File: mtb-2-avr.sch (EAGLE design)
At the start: 1 part

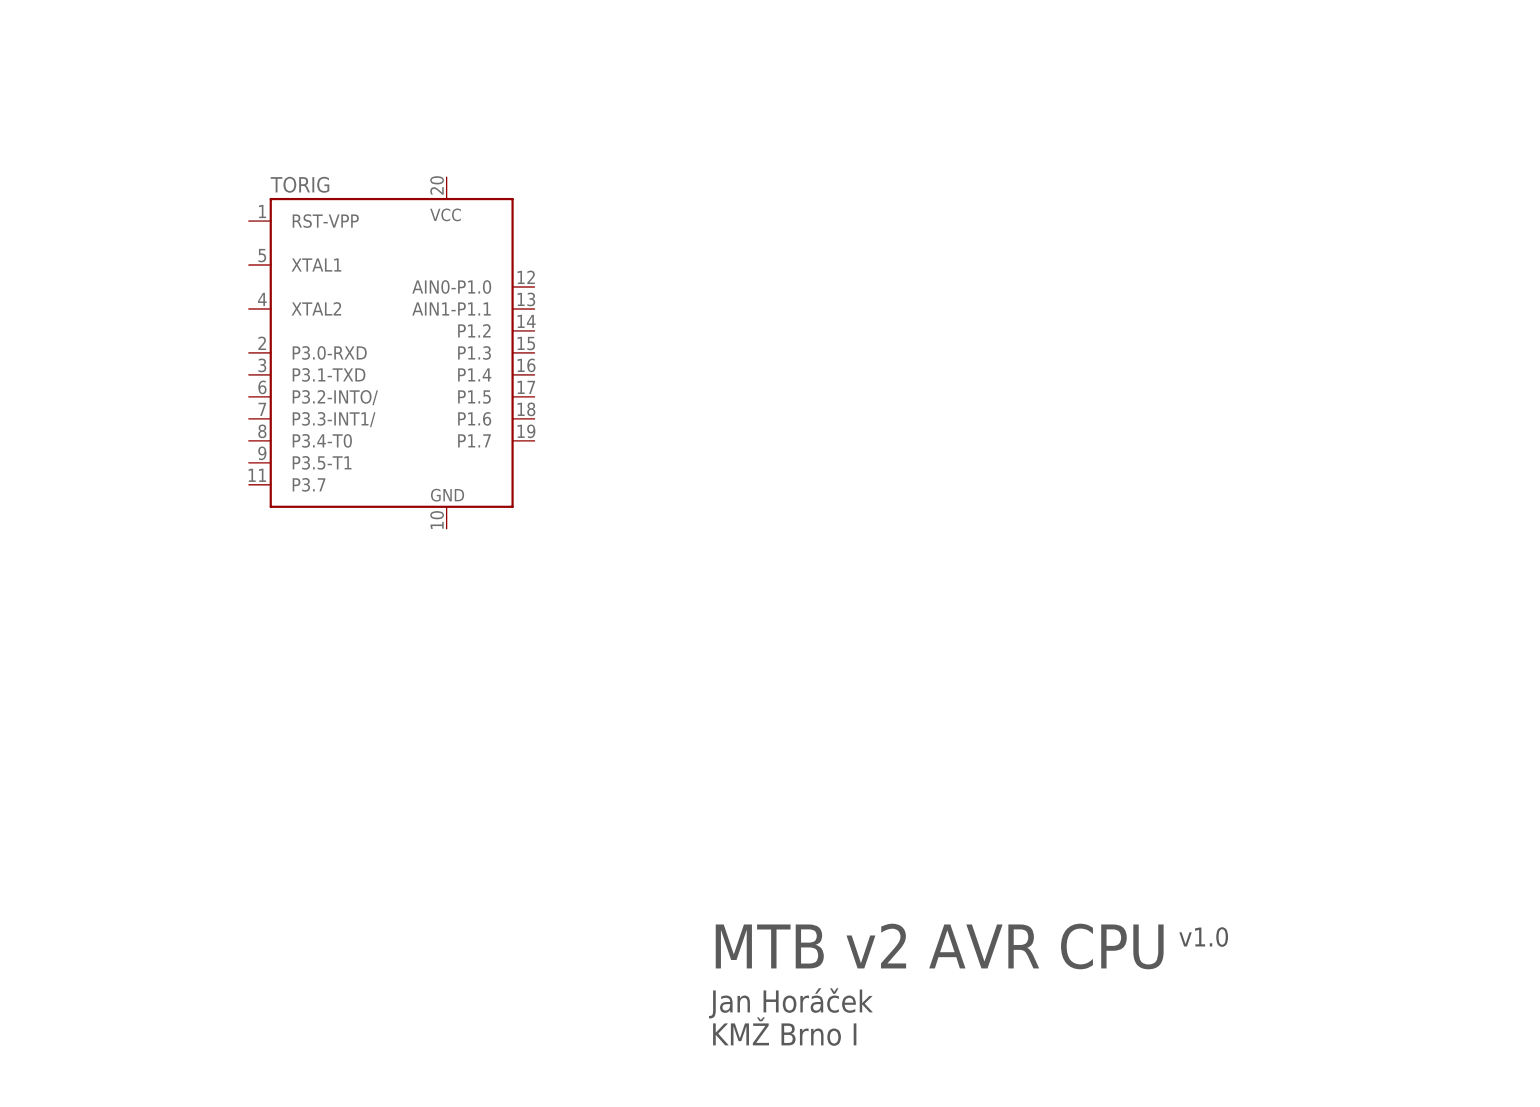
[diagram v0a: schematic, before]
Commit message: Add wires to schematics, create pcb template.
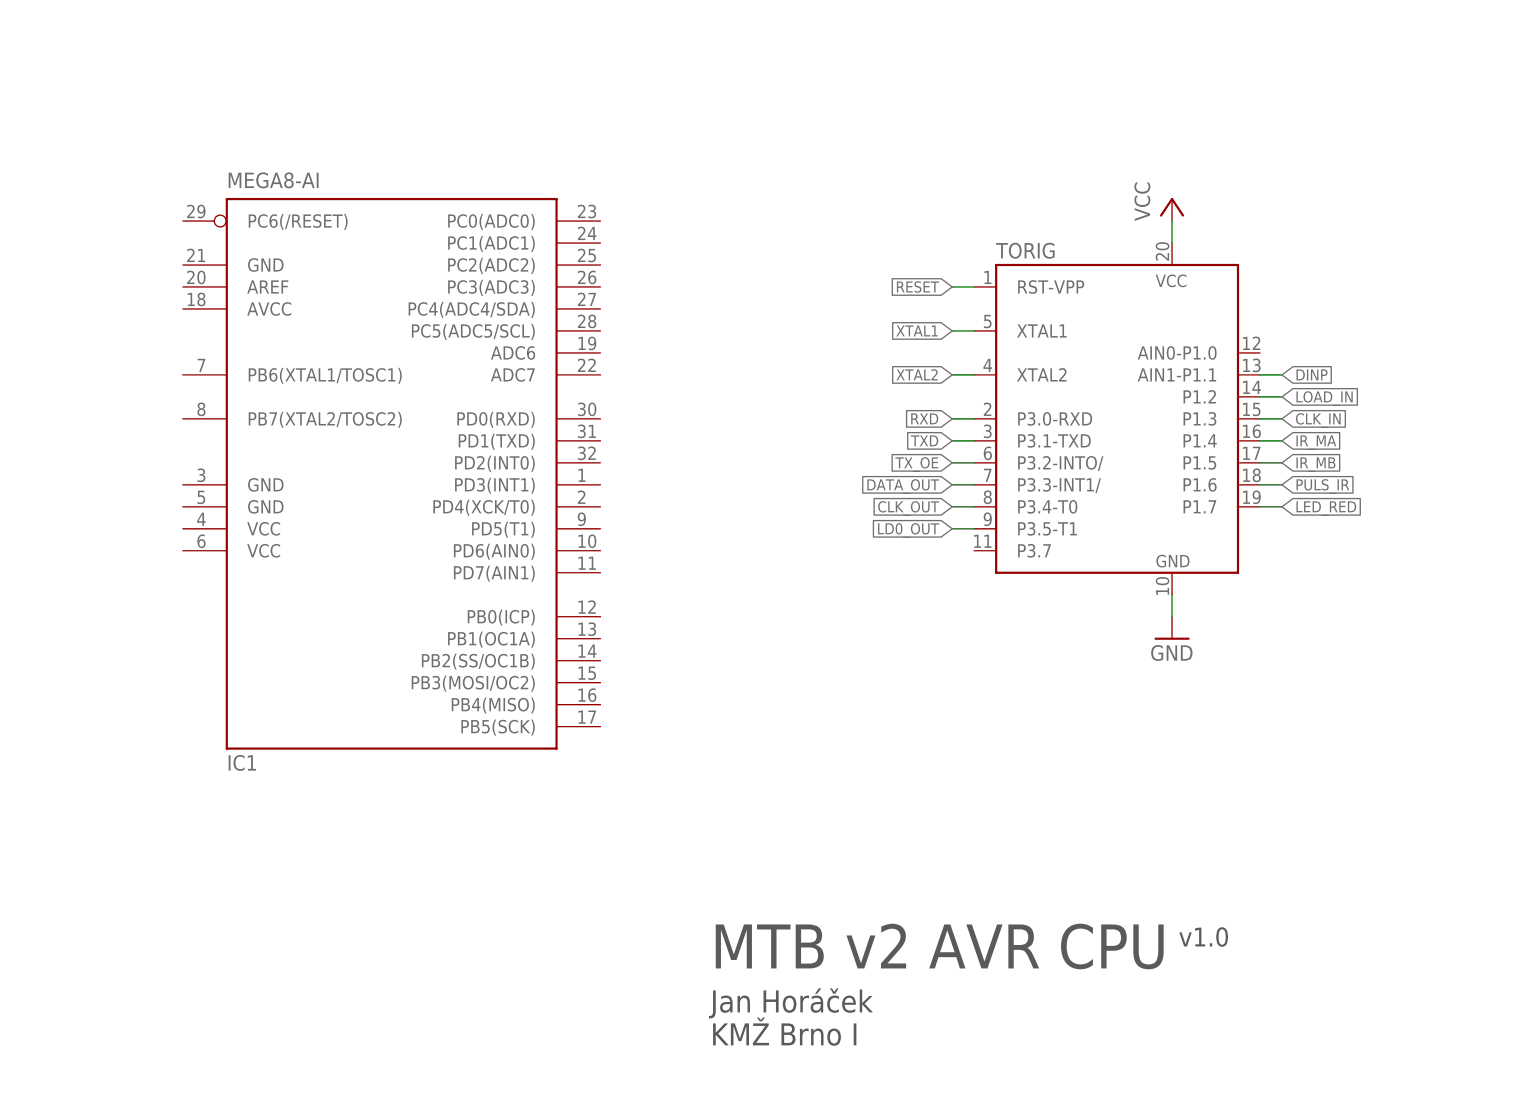
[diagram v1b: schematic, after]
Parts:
- added IC1: MEGA8-AI, atmel:MEGA8-AI
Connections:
- new net CLK_IN: TORIG.P1.3
- new net CLK_OUT: TORIG.P3.4-T0
- new net DATA_OUT: TORIG.P3.3-INT1/
- new net DINP: TORIG.AIN1-P1.1
- new net GND: TORIG.GND
- new net IR_MA: TORIG.P1.4
- new net IR_MB: TORIG.P1.5
- new net LD0_OUT: TORIG.P3.5-T1
- new net LED_RED: TORIG.P1.7
- new net LOAD_IN: TORIG.P1.2
- new net PULS_IR: TORIG.P1.6
- new net RESET: TORIG.RST-VPP
- new net RXD: TORIG.P3.0-RXD
- new net TXD: TORIG.P3.1-TXD
- new net TX_OE: TORIG.P3.2-INTO/
- new net VCC: TORIG.VCC
- new net XTAL1: TORIG.XTAL1
- new net XTAL2: TORIG.XTAL2
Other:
- moved on the sheet: TORIG

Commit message: Sch: connect must-signals.
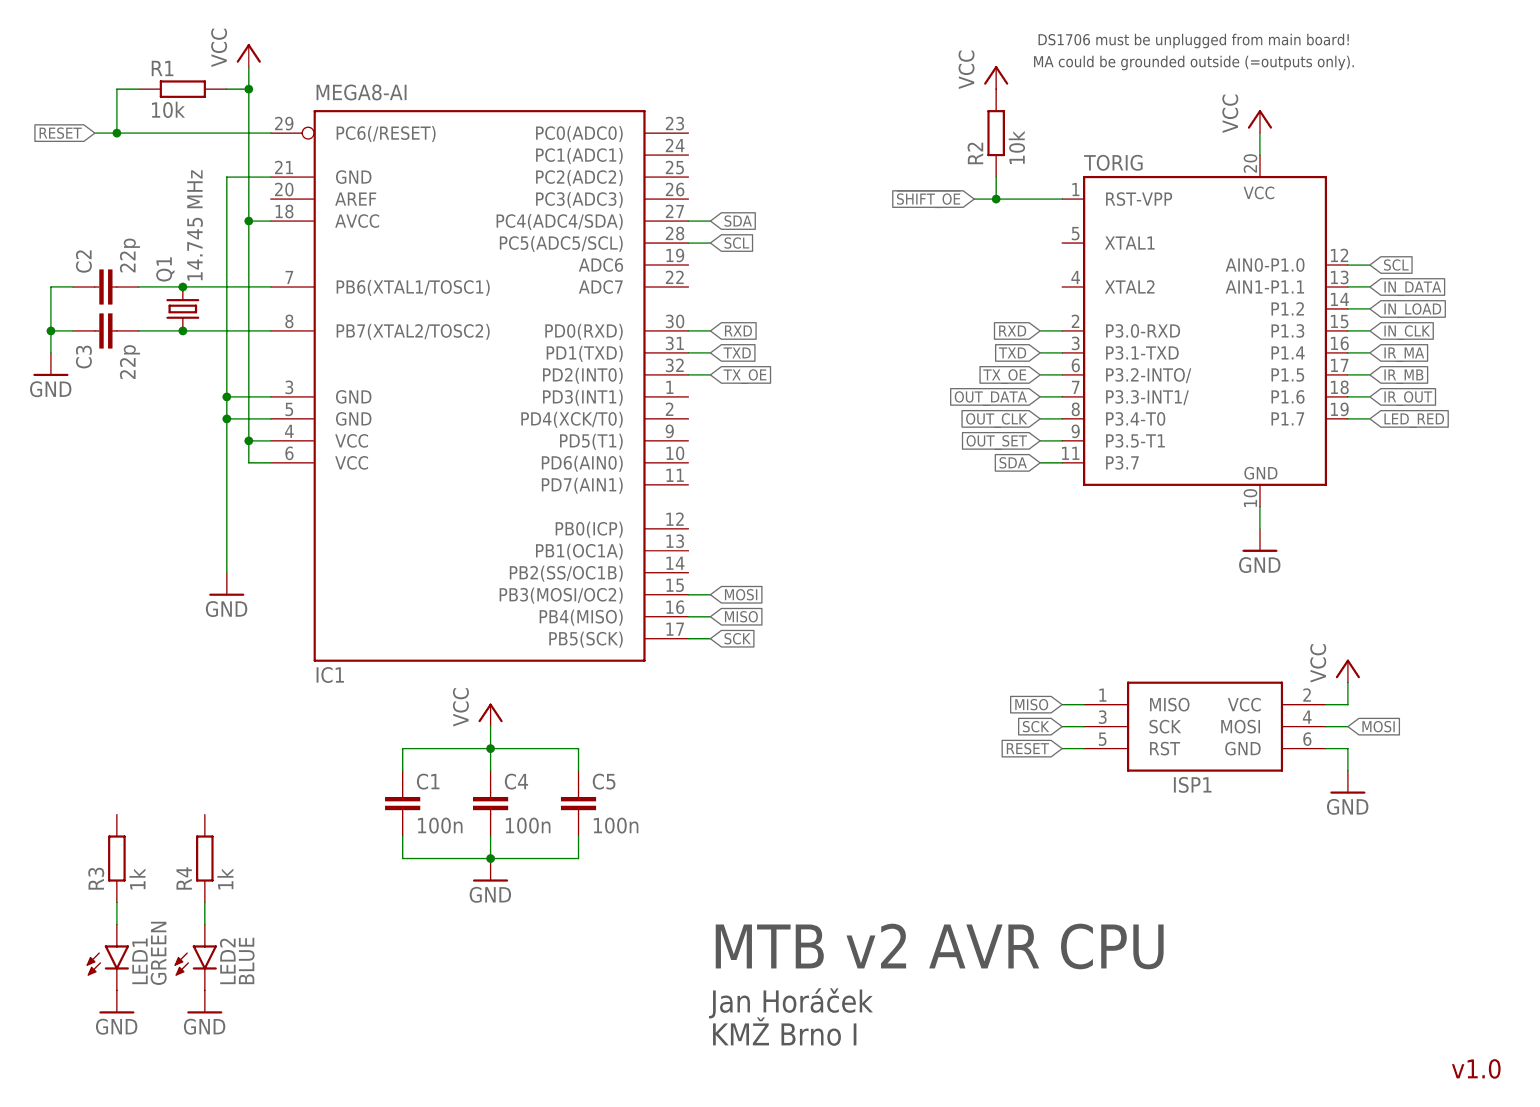
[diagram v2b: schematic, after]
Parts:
- added C1, C4, C5: 100n, rcl:C-EUC0805
- added C2, C3: 22p, rcl:C-EUC0805
- added ISP1: AVRISP-6, adafruit:AVRISP-6
- added LED1: GREEN, led:LEDCHIPLED_0805
- added LED2: BLUE, led:LEDCHIPLED_0805
- added Q1: 14.745 MHz, crystal:CRYSTALHC49UP
- added R1, R2: 10k, rcl:R-EU_R0805
- added R3, R4: 1k, rcl:R-EU_R0805
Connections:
- net CLK_IN renamed IN_CLK
- net CLK_OUT renamed OUT_CLK
- net DATA_OUT renamed OUT_DATA
- net DINP renamed IN_DATA
- net LD0_OUT renamed OUT_SET
- net LOAD_IN renamed IN_LOAD
- net PULS_IR renamed IR_OUT
- removed net XTAL1: TORIG.XTAL1
- removed net XTAL2: TORIG.XTAL2
- new net !SHIFT_OE: R2.1, TORIG.RST-VPP
- new net MISO: IC1.PB4(MISO), ISP1.MISO
- new net MOSI: IC1.PB3(MOSI/OC2), ISP1.MOSI
- new net N$1: C2.2, IC1.PB6(XTAL1/TOSC1), Q1.2
- new net N$2: C3.2, IC1.PB7(XTAL2/TOSC2), Q1.1
- new net N$3: LED1.A, R3.1
- new net N$4: LED2.A, R4.1
- new net SCK: IC1.PB5(SCK), ISP1.SCK
- new net SCL: IC1.PC5(ADC5/SCL), TORIG.AIN0-P1.0
- new net SDA: IC1.PC4(ADC4/SDA), TORIG.P3.7
- net GND: now also C1.2, C2.1, C3.1, C4.2, C5.2, IC1.GND, IC1.GND@1, IC1.GND@2, ISP1.GND, LED1.C, LED2.C
- net RESET: now also IC1.PC6(/RESET), ISP1.RST, R1.1; no longer TORIG.RST-VPP
- net RXD: now also IC1.PD0(RXD)
- net TXD: now also IC1.PD1(TXD)
- net TX_OE: now also IC1.PD2(INT0)
- net VCC: now also C1.1, C4.1, C5.1, IC1.AVCC, IC1.VCC@1, IC1.VCC@2, ISP1.VCC, R1.2, R2.2
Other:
- note added: "DS1706 must be unplugged from main board!"
- note added: "MA could be grounded outside (=outputs only)."
- moved on the sheet: IC1, TORIG

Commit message: Connect all wires.
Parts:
- removed C5: 100n, rcl:C-EUC0805
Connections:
- removed net IN_CLK: TORIG.P1.3
- removed net IN_DATA: TORIG.AIN1-P1.1
- removed net OUT_CLK: TORIG.P3.4-T0
- removed net OUT_DATA: TORIG.P3.3-INT1/
- new net LED_BLUE: R4.2
- new net LED_GREEN: R3.2
- net GND: no longer C5.2
- net IN_LOAD: now also IC1.ADC6
- net IR_MA: now also IC1.PC3(ADC3)
- net IR_MB: now also IC1.PC2(ADC2)
- net IR_OUT: now also IC1.PC1(ADC1)
- net LED_RED: now also IC1.PC0(ADC0)
- net MISO: now also TORIG.AIN1-P1.1
- net MOSI: now also TORIG.P3.3-INT1/
- net OUT_SET: now also IC1.PD3(INT1)
- net SCK: now also TORIG.P1.3, TORIG.P3.4-T0
- net VCC: no longer C5.1
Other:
- note added: "IN_CLK"
- note added: "IN_DATA"
- note added: "OUT_CLK"
- note added: "OUT_DATA"
- moved on the sheet: C1, C4, R2, TORIG

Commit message: Route everything.
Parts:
- C1, C2, C3, C4: device rcl:C-EUC0805 -> rcl:C-EUC0603
- LED1, LED2: device led:LEDCHIPLED_0805 -> led:LEDCHIPLED_0603
- R1, R2, R3, R4: device rcl:R-EU_R0805 -> rcl:R-EU_R0603
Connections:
- net LED_BLUE: now also IC1.PB1(OC1A)
- net LED_GREEN: now also IC1.PB0(ICP)
